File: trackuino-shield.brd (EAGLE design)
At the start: 67.3 x 53.3 mm, 26 parts, among them IC2 REG1117, IC3 ON M74VHC1GT125DT1G, IC4 ON M74VHC1GT125DT1G, IC5 ON M74VHC1GT125DT1G, J5 J5MM, J6 J5MM, J7 J5MM, J8 J5MM, M2 HX1, Q1 PMV20XN, PMV16UN, etc, U1 LM60 int, X1 BU-SMA-V, X2 Vin, X3 LM60 ext, X4 Buzzer

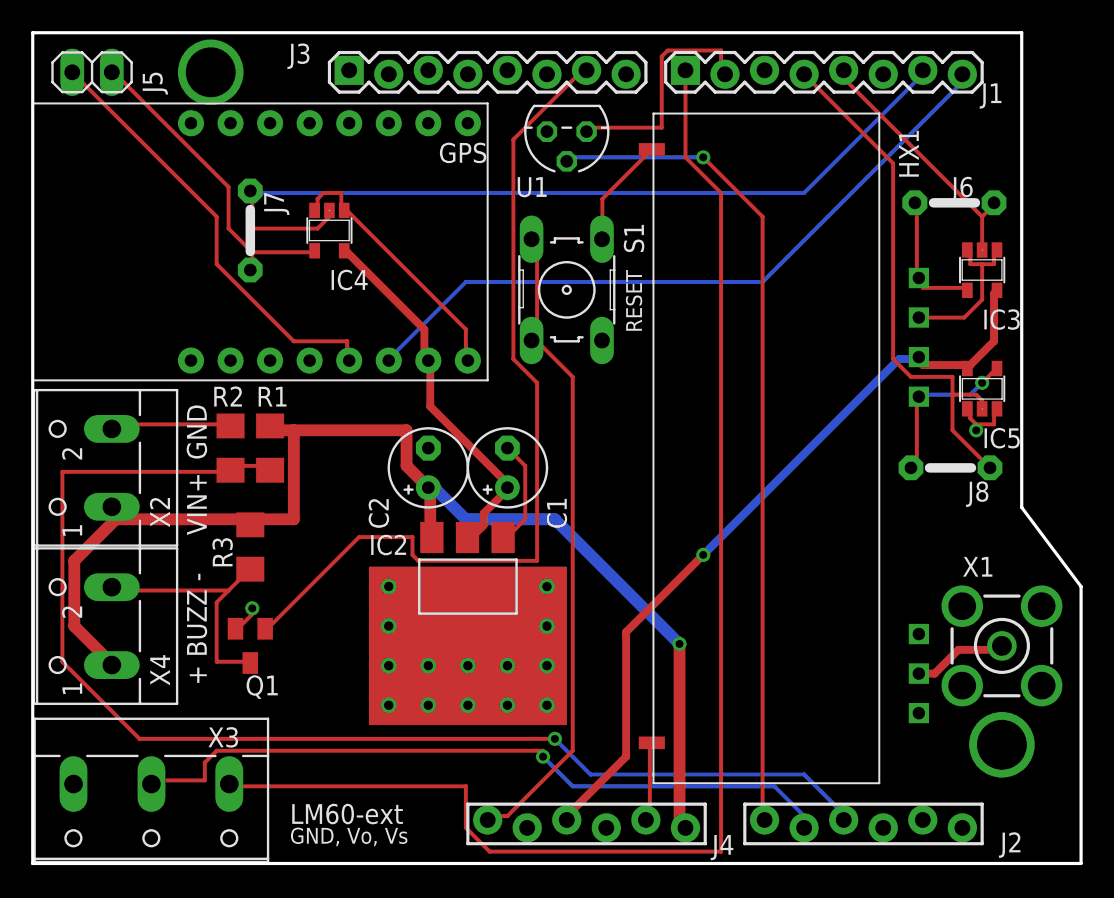
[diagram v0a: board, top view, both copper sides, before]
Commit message: removing the level shifters
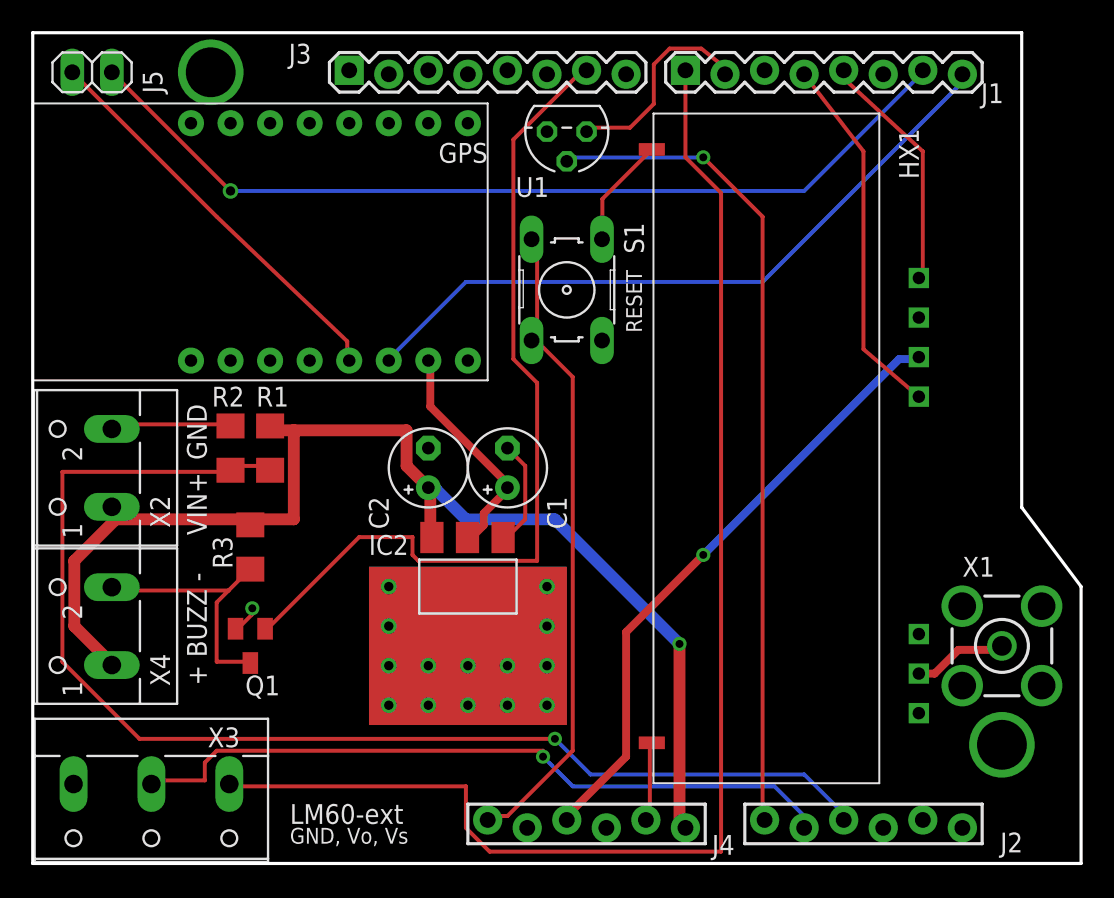
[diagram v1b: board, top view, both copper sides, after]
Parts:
- removed IC3, IC4, IC5: ON M74VHC1GT125DT1G, 74xx-little-us:SOT23-5
- removed J6, J7, J8: J5MM, jumper:05
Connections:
- removed net EN-5V: IC5.4, J8.2, M2.EN
- removed net TX-3V3: IC4.4, J5.2, J7.2
- removed net TXD-5V: IC3.4, J6.2, M2.TXD
- net +3V3: no longer IC4.5
- net +5V: no longer IC3.5, IC5.5
- net D3: now also M2.TXD; no longer IC3.2, J6.1
- net D4: now also M2.EN; no longer IC5.2, J8.1
- net GND: no longer IC3.1, IC3.3, IC4.1, IC4.3, IC5.1, IC5.3
- net TX: now also J5.2; no longer IC4.2, J7.1
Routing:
- net GND: track 59.6 -> 28.9 mm, vias 2 -> 1
- net TX-3V3: track 20.6 -> 0.00 mm
- net D4: track 34.4 -> 23.6 mm
- net EN-5V: track 10.5 -> 0.00 mm, vias 1 -> 0
- net +5V: track 49.2 -> 39.8 mm
- net +3V3: track 24.0 -> 14.9 mm
- net TXD-5V: track 8.59 -> 0.00 mm
- net TX: track 54.8 -> 58.5 mm, vias 0 -> 1
- net D6: track 15.2 -> 13.0 mm
- net N$2: track 27.9 -> 26.0 mm
- net D3: track 16.4 -> 15.6 mm

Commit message: Successfully replaced all surface mount components.
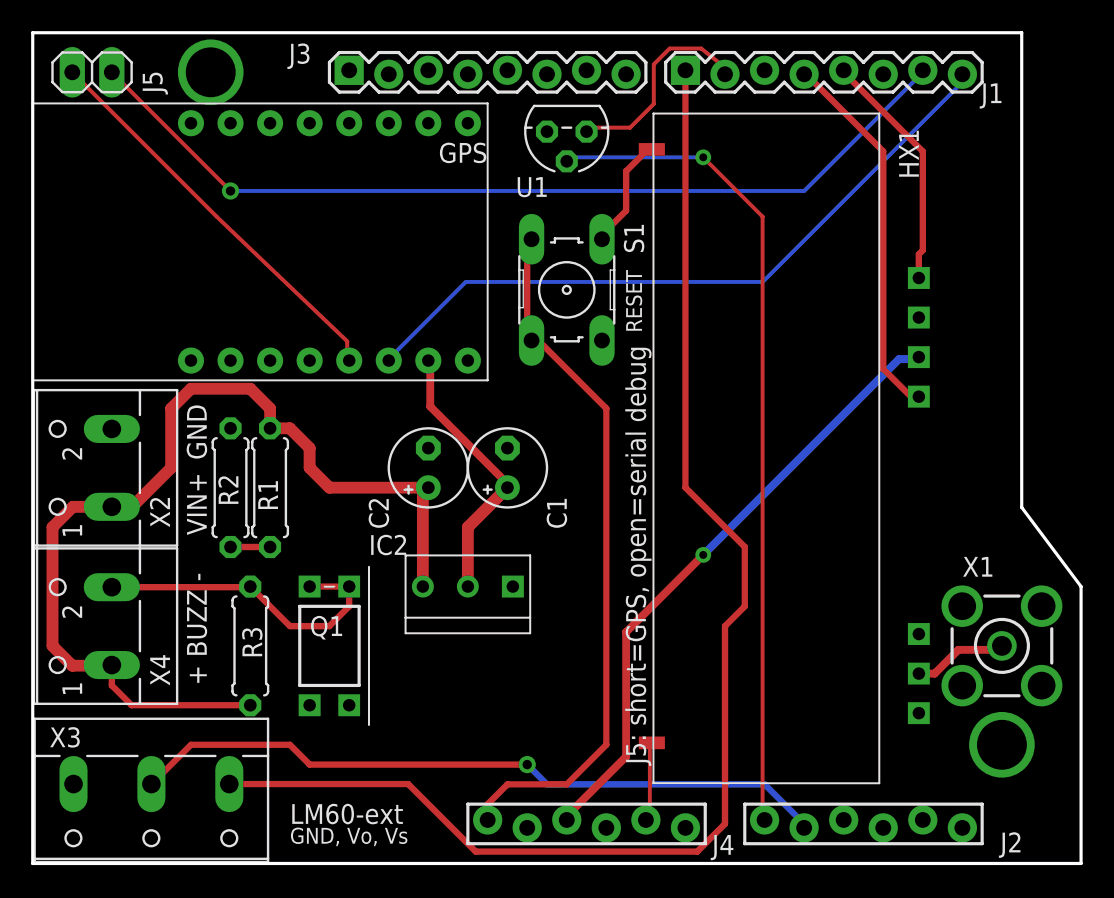
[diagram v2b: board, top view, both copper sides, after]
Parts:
- IC2: value REG1117 -> AP1117; device burr-brown:SOT223 -> First:TO220-3
- Q1: value PMV20XN, PMV16UN, etc -> IRLD110IRLD110; device transistor-small-signal:SOT23 -> First:HVMDIP
- R1, R2, R3: device resistor:R1206 -> rcl:0207/7
- moved R3 6.35 mm to (14.0, 14.0), turned to 270 degrees
- moved Q1 5.39 mm to (17.8, 17.8)
- moved R1 2.54 mm to (15.2, 24.1)
- moved R2 2.54 mm to (12.7, 24.1)
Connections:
- net D9: no longer Q1.1
- net GND: now also Q1.S; no longer Q1.2
- net N$1: now also Q1.D@1, Q1.D@2; no longer Q1.3
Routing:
- net A2: track 80.6 -> 2.54 mm, vias 1 -> 0
- net D9: track 55.5 -> 0.00 mm
- net GND: track 28.9 -> 12.4 mm, vias 1 -> 0
- net VIN: track 79.8 -> 63.4 mm, vias 1 -> 0
- net N$1: track 16.6 -> 20.6 mm
- net RESET: track 41.9 -> 45.7 mm
- net +3V3: track 14.9 -> 17.9 mm
- net D7: track 86.0 -> 84.9 mm
- net A1: track 46.3 -> 45.3 mm
- net D4: track 23.6 -> 24.2 mm

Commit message: Placed buzzer mosfet. All surface mount components have been removed
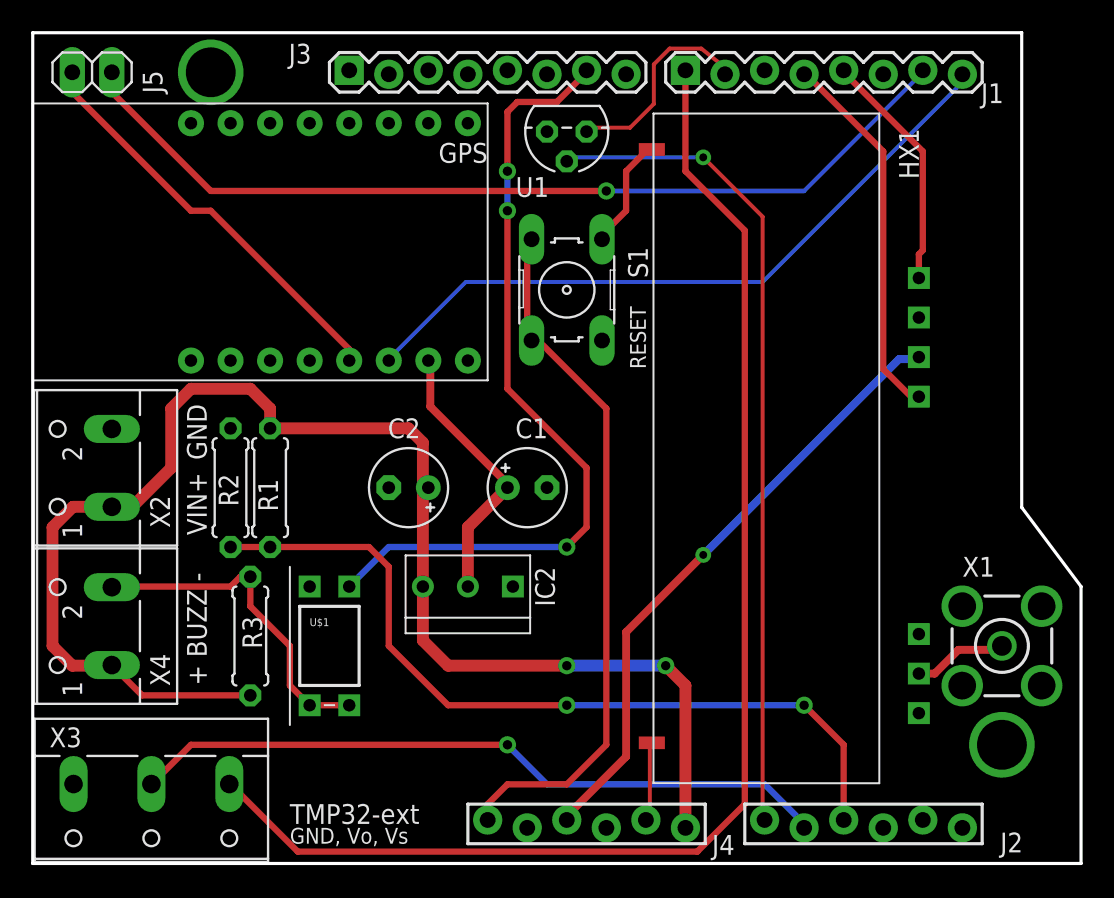
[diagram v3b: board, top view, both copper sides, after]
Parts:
- removed Q1: IRLD110IRLD110, First:HVMDIP
- added U$1: IRLD110IRLD110, First:HVMDIP
- moved C1 1.80 mm to (31.8, 24.1), turned to 0 degrees
- moved C2 1.80 mm to (24.1, 24.1), turned to 180 degrees
- moved R3 0.63 mm to (14.0, 14.6)
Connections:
- net D9: now also U$1.G
- net GND: now also U$1.S; no longer Q1.S
- net N$1: now also U$1.D@1, U$1.D@2; no longer Q1.D@1, Q1.D@2
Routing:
- net D9: track 0.00 -> 51.9 mm, vias 0 -> 3
- net A2: track 2.54 -> 52.4 mm, vias 0 -> 2
- net VIN: track 63.4 -> 93.9 mm, vias 0 -> 2
- net A1: track 45.3 -> 47.1 mm
- net N$1: track 20.6 -> 21.5 mm
- net TX: track 58.5 -> 59.3 mm
- net N$2: track 26.0 -> 26.6 mm
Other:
- board text added: "TMP32-ext"
- board text removed: "J5: short=GPS, open=serial debug"
- board text removed: "LM60-ext"

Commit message: Minor routing change
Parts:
- renumbered U$1 to Q1
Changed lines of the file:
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@@
 <attribute name="VALUE" x="29.21" y="29.75" size="1.27" layer="27" rot="R180"/>
 </element>
-<element name="U$1" library="First" package="HVMDIP" value="IRLD110IRLD110" x="20.32" y="10.16"/>
+<element name="Q1" library="First" package="HVMDIP" value="IRLD110IRLD110" x="20.32" y="10.16" smashed="yes">
+<attribute name="NAME" x="17.78" y="14.605" size="1.27" layer="25" font="vector"/>
+<attribute name="VALUE" x="17.78" y="12.7" size="0.508" layer="27" font="vector"/>
+</element>
 </elements>
 <signals>
@@
 <wire x1="36.83" y1="40.64" x2="36.83" y2="40.3606" width="0.4064" layer="1"/>
 <wire x1="36.83" y1="40.3606" x2="36.5506" y2="40.0812" width="0.4064" layer="1"/>
-<contactref element="U$1" pad="S"/>
+<contactref element="Q1" pad="S"/>
 </signal>
 <signal name="+5V" class="2">
@@
 <signal name="D9">
 <contactref element="J3" pad="7"/>
-<contactref element="U$1" pad="G"/>
+<contactref element="Q1" pad="G"/>
 <wire x1="35.56" y1="50.927" x2="35.56" y2="50.8" width="0.4064" layer="1"/>
 <wire x1="35.56" y1="50.8" x2="33.655" y2="48.895" width="0.4064" layer="1"/>
@@
 <contactref element="X4" pad="2"/>
 <contactref element="R3" pad="1"/>
-<contactref element="U$1" pad="D@1"/>
-<contactref element="U$1" pad="D@2"/>
+<contactref element="Q1" pad="D@1"/>
+<contactref element="Q1" pad="D@2"/>
 <wire x1="20.32" y1="10.16" x2="17.78" y2="10.16" width="0.4064" layer="1"/>
 <wire x1="17.78" y1="10.16" x2="16.51" y2="11.43" width="0.4064" layer="1"/>

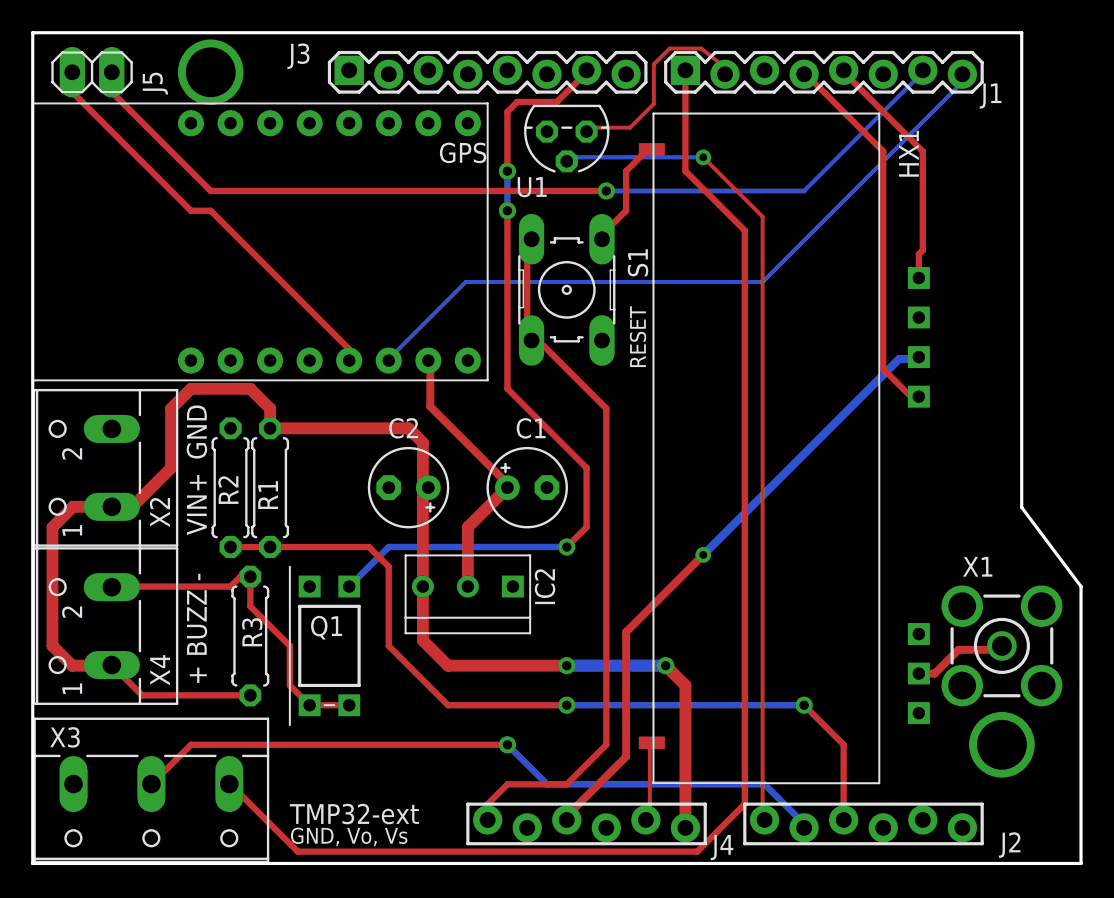
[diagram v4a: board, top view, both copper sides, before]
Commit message: Reorg schematic and removed TX to GPS
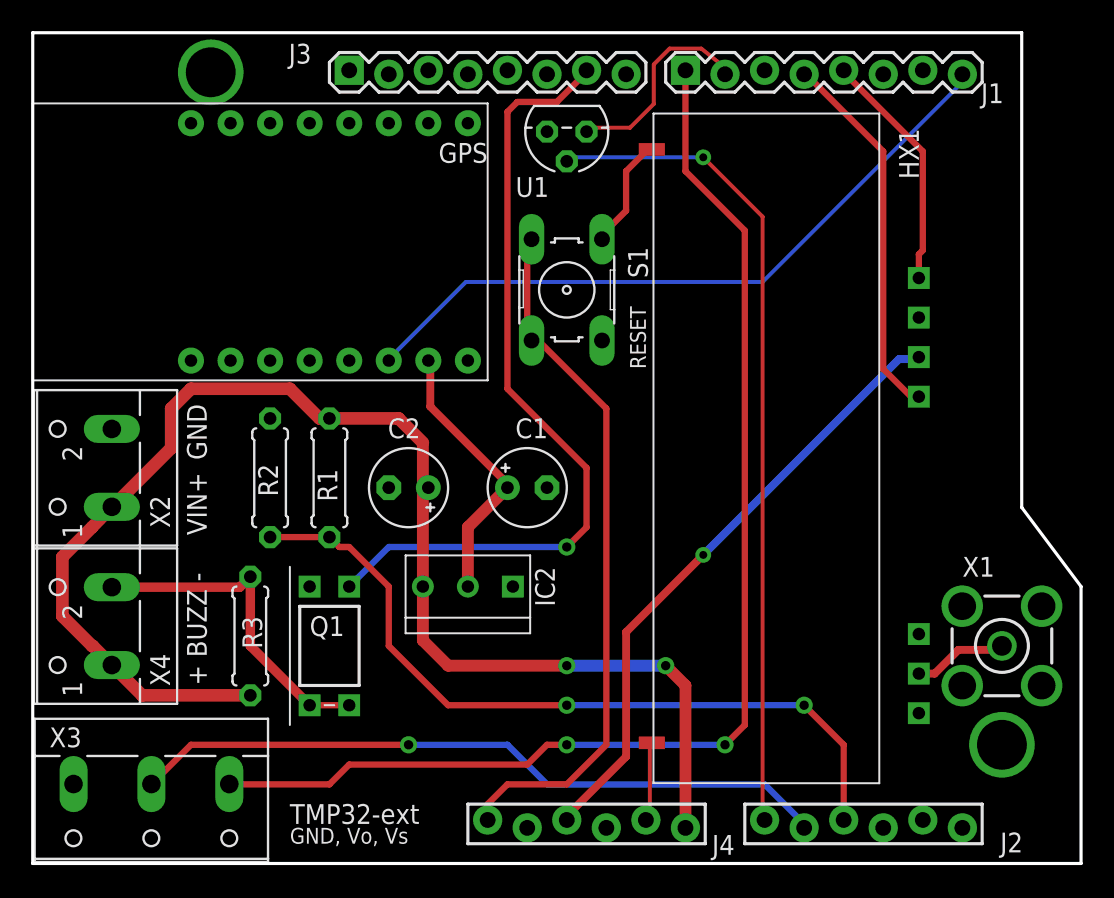
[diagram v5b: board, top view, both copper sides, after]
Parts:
- removed J5: J5MM, pinhead:1X02
- Q1: value IRLD110IRLD110 -> IRLD110; device First:HVMDIP -> trackuino:HVMDIP
- moved R1 3.86 mm to (19.1, 24.8)
- moved R2 2.62 mm to (15.2, 24.8)
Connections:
- removed net N$2: GPS.RX0, J5.1
- net GND: now also GPS.RX0
- net TX: no longer J5.2
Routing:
- net TX: track 59.3 -> 0.00 mm, vias 1 -> 0
- net N$2: track 26.6 -> 0.00 mm
- net D7: track 84.9 -> 78.3 mm, vias 0 -> 2
- net VIN: track 93.9 -> 88.9 mm
- net A2: track 52.4 -> 49.4 mm
- net A1: track 47.1 -> 45.3 mm
- net D9: vias 3 -> 1

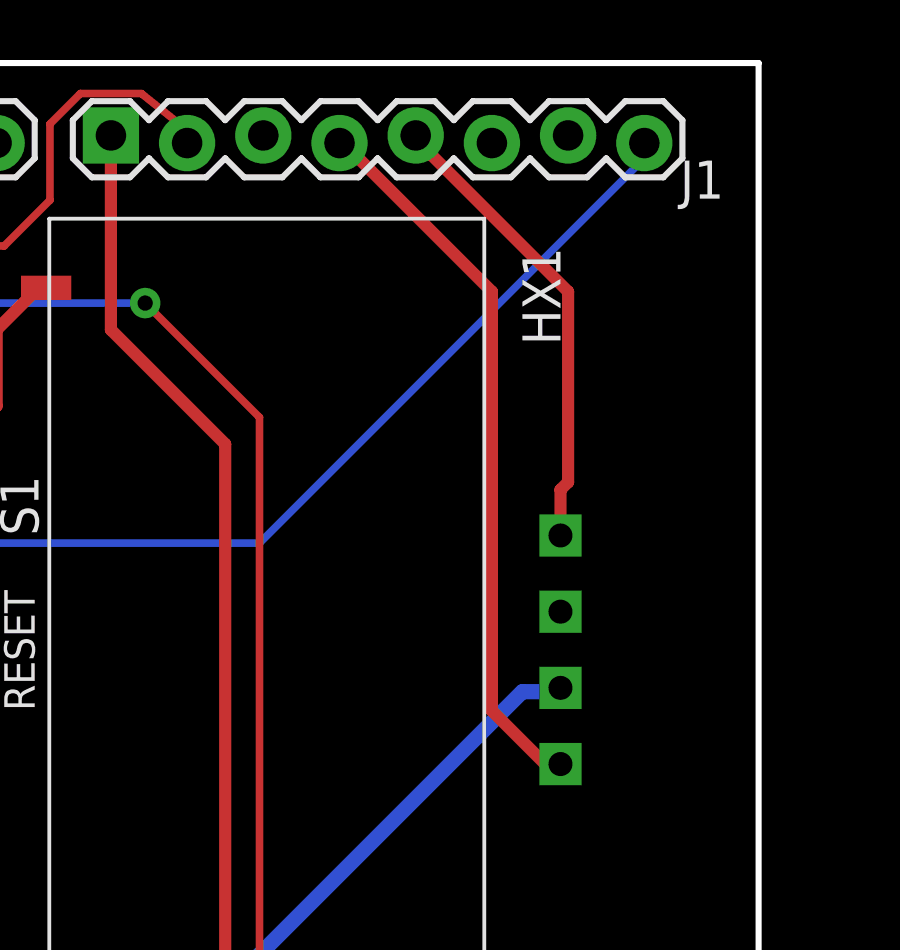
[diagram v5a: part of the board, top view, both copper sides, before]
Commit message: Fixed an airwire
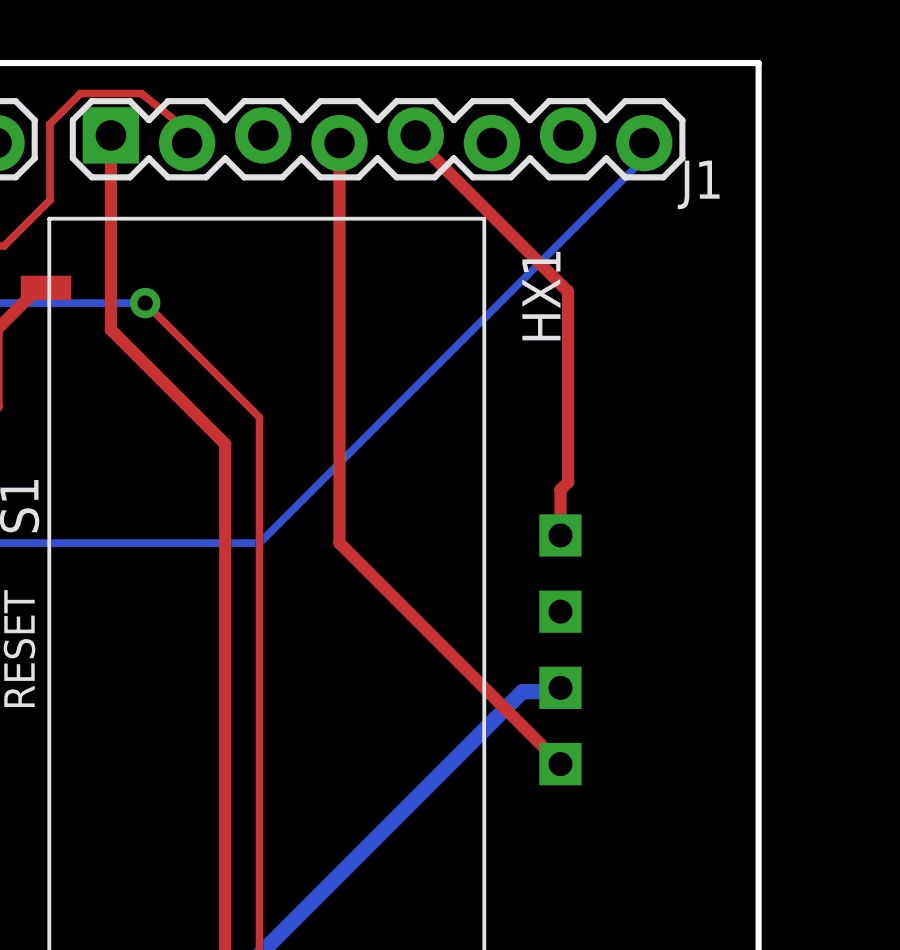
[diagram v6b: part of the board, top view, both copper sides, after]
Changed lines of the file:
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@@
 <contactref element="J1" pad="4"/>
 <contactref element="M2" pad="EN"/>
-<wire x1="56.896" y1="29.972" x2="56.388" y2="29.972" width="0.4064" layer="1"/>
-<wire x1="56.388" y1="29.972" x2="54.61" y2="31.75" width="0.4064" layer="1"/>
-<wire x1="54.61" y1="31.75" x2="54.61" y2="45.72" width="0.4064" layer="1"/>
-<wire x1="54.61" y1="45.72" x2="49.53" y2="50.8" width="0.4064" layer="1"/>
-<wire x1="49.53" y1="50.8" x2="49.53" y2="50.673" width="0" layer="19" extent="1-1"/>
+<wire x1="56.896" y1="29.972" x2="49.53" y2="37.338" width="0.4064" layer="1"/>
+<wire x1="49.53" y1="37.338" x2="49.53" y2="50.673" width="0.4064" layer="1"/>
 </signal>
 <signal name="D5">
